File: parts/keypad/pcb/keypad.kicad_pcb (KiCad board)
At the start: 2 copper layers, 95 x 74.5 mm, 22 parts, among them J1 Conn_02x10_Top_Bottom, J2 1x10, J3 To SENSOR HUB, J4 To DISPLAY MODULE, SW1 SW_Push, SW10 SW_Push, SW2 SW_Push, SW3 SW_Push, SW4 SW_Push, SW5 SW_Push, SW6 SW_Push, SW7 SW_Push, SW8 SW_Push, SW9 SW_Push

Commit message: update connector to hub to match hub pinouts
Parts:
- removed J3: To SENSOR HUB, Connector_PinHeader_2.54mm:PinHeader_1x04_P2.54mm_Horizontal
- added TO_HUB1: Conn_01x05, Connector_PinHeader_2.54mm:PinHeader_1x05_P2.54mm_Horizontal, B.Cu at (56.8, 96.2)
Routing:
- net Net-(J2-SCL): track 107.3 -> 94.9 mm, vias 1 -> 0
- net /N$3: track 61.2 -> 52.3 mm, vias 1 -> 0
- net /GND: track 298.3 -> 290.0 mm, vias 0 -> 1
- net /N$2: track 81.3 -> 76.0 mm
- net Net-(J2-SDA): track 95.0 -> 91.8 mm
- net /N$5: track 93.9 -> 97.0 mm
- net Net-(J2-3V3): track 124.3 -> 121.5 mm
- net /N$10: track 18.8 -> 16.6 mm
- net /N$8: track 58.5 -> 56.4 mm
- net /N$9: track 24.1 -> 25.2 mm
- net /N$6: track 77.5 -> 76.7 mm
- net /N$1: track 99.0 -> 99.5 mm
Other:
- board text added: "(C) 2026 ARKADIA HOUSE Keypad Display rev 01.7"
- board text added: "3V3 nc GND SDA SCL"
- board text added: "To HUB"
- board text removed: "(C) 2026 ARKADIA HOUSE Keypad Display rev 01.6"
- board text removed: "SCL SDA 3V3 GND"

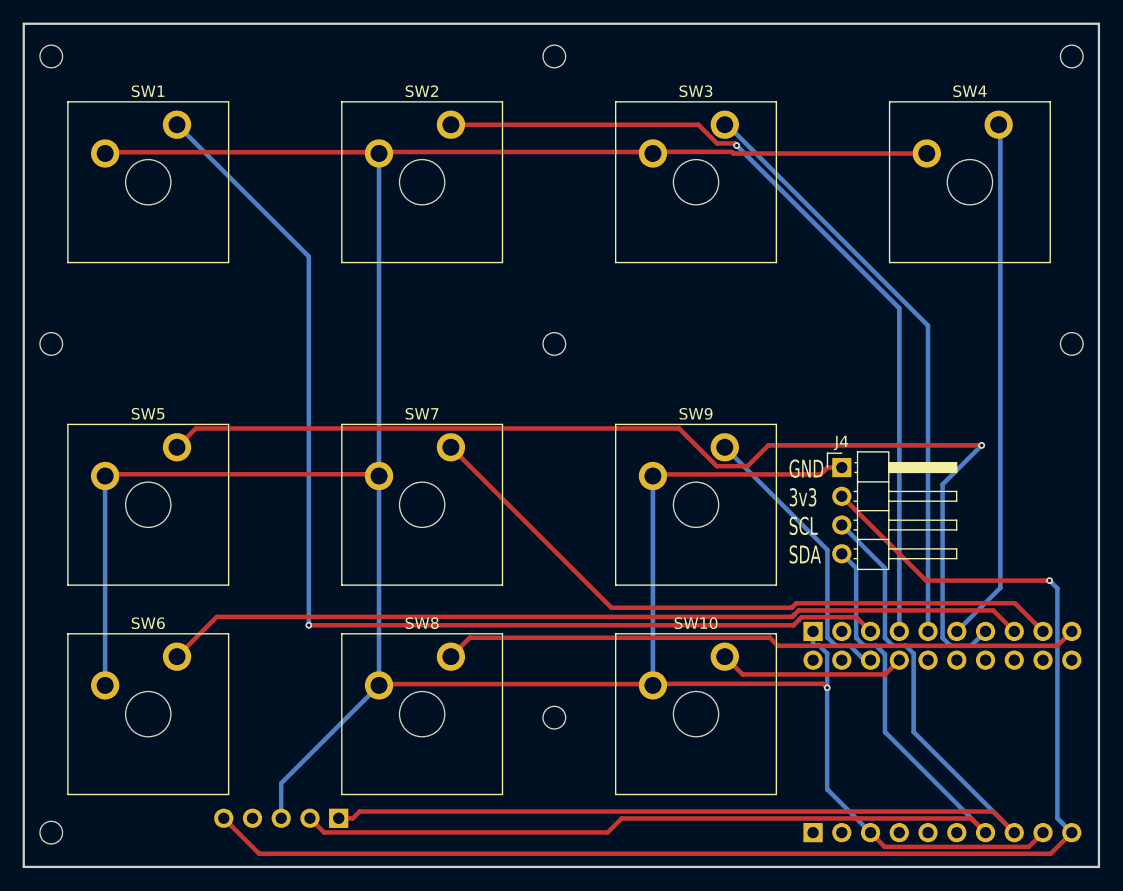
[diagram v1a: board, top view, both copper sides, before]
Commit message: cleaned up vias and tracks
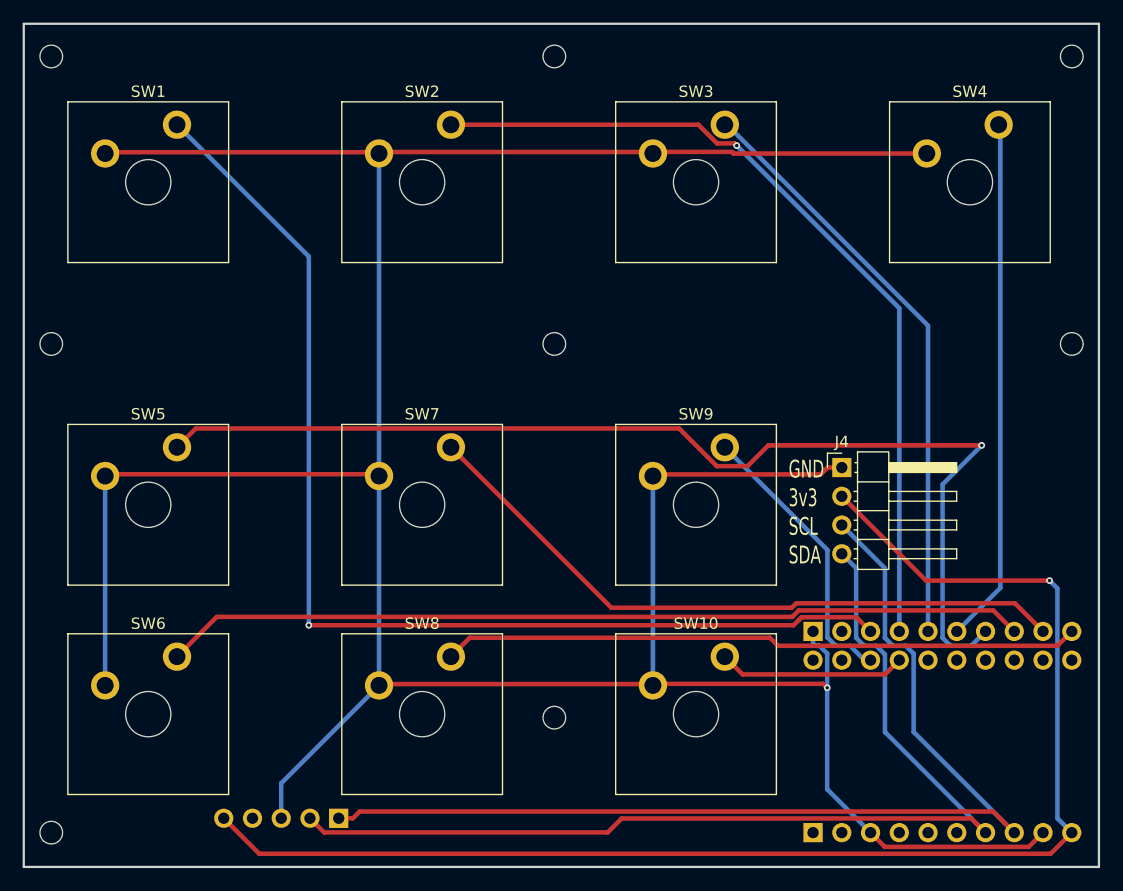
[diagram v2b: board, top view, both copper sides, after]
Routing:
- net /GND: track 290.0 -> 287.9 mm
- net /N$2: track 76.0 -> 74.9 mm
- net /N$9: track 25.2 -> 24.7 mm
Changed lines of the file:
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@@
 			(crossoutdnponfab yes)
 			(subtractmaskfromsilk no)
-			(outputformat 3)
+			(outputformat 1)
 			(mirror no)
-			(drillshape 2)
+			(drillshape 0)
 			(scaleselection 1)
 			(outputdirectory "../fab/")
@@
 	)
 	(segment
-		(start 84.7282 84.3218)
-		(end 84.59 84.46)
-		(width 0.4)
-		(layer "F.Cu")
-		(net "/GND")
-	)
-	(segment
 		(start 84.7282 37.3218)
 		(end 91.5627 37.3218)
@@
 	)
 	(segment
-		(start 60.5239 37.3261)
-		(end 60.39 37.46)
-		(width 0.4)
-		(layer "F.Cu")
-		(net "/GND")
-	)
-	(segment
 		(start 84.7363 65.8137)
 		(end 99.4266 65.8137)
@@
 	)
 	(segment
-		(start 84.59 65.96)
-		(end 84.7363 65.8137)
-		(width 0.4)
-		(layer "F.Cu")
-		(net "/GND")
-	)
-	(segment
 		(start 101.28 65.212)
 		(end 100.0283 65.212)
@@
 	)
 	(segment
-		(start 84.4783 84.3483)
-		(end 84.59 84.46)
-		(width 0.4)
-		(layer "F.Cu")
-		(net "/GND")
-	)
-	(segment
 		(start 84.4561 37.3261)
 		(end 60.5239 37.3261)
@@
 	)
 	(segment
-		(start 60.39 84.46)
-		(end 60.5017 84.3483)
-		(width 0.4)
-		(layer "F.Cu")
-		(net "/GND")
-	)
-	(segment
-		(start 84.59 37.46)
-		(end 84.4561 37.3261)
-		(width 0.4)
-		(layer "F.Cu")
-		(net "/GND")
-	)
-	(segment
 		(start 60.5017 84.3483)
 		(end 84.4783 84.3483)
@@
 	)
 	(segment
-		(start 108.7834 37.4666)
-		(end 108.79 37.46)
-		(width 0.4)
-		(layer "F.Cu")
-		(net "/GND")
-	)
-	(segment
 		(start 99.6392 84.3218)
 		(end 84.7282 84.3218)
@@
 	)
 	(segment
-		(start 36.19 65.96)
-		(end 36.3483 65.8017)
-		(width 0.4)
-		(layer "F.Cu")
-		(net "/GND")
-	)
-	(segment
 		(start 99.9917 84.6743)
 		(end 99.6392 84.3218)
@@
 	)
 	(segment
-		(start 60.2317 65.8017)
-		(end 60.39 65.96)
-		(width 0.4)
-		(layer "F.Cu")
-		(net "/GND")
-	)
-	(segment
 		(start 36.3483 65.8017)
 		(end 60.2317 65.8017)
@@
 	)
 	(segment
-		(start 60.2783 37.3483)
-		(end 60.39 37.46)
-		(width 0.4)
-		(layer "F.Cu")
-		(net "/GND")
-	)
-	(segment
 		(start 91.5627 37.3218)
 		(end 91.7075 37.4666)
@@
 		(net "/GND")
 	)
-	(segment
-		(start 36.19 37.46)
-		(end 36.3017 37.3483)
-		(width 0.4)
-		(layer "F.Cu")
-		(net "/GND")
-	)
-	(segment
-		(start 84.59 37.46)
-		(end 84.7282 37.3218)
-		(width 0.4)
-		(layer "F.Cu")
-		(net "/GND")
-	)
 	(via
 		(at 99.9917 84.6743)
@@
 	)
 	(segment
-		(start 91.8048 36.5717)
-		(end 91.998 36.7649)
-		(width 0.4)
-		(layer "F.Cu")
-		(net "/N$2")
-	)
-	(segment
 		(start 90.2559 36.5717)
 		(end 91.8048 36.5717)
@@
 	)
 	(segment
-		(start 91.8048 36.5717)
-		(end 91.998 36.7649)
-		(width 0.4)
-		(layer "F.Cu")
-		(net "/N$2")
-	)
-	(segment
 		(start 91.998 36.7649)
 		(end 91.8048 36.5717)
@@
 	)
 	(segment
-		(start 91.998 36.7649)
-		(end 91.8048 36.5717)
-		(width 0.4)
-		(layer "B.Cu")
-		(net "/N$2")
-	)
-	(segment
-		(start 91.8048 36.5717)
-		(end 91.998 36.7649)
-		(width 0.4)
-		(layer "B.Cu")
-		(net "/N$2")
-	)
-	(segment
 		(start 106.36 51.1269)
 		(end 106.36 79.69)
@@
 	)
 	(segment
-		(start 91.1454 34.92)
-		(end 90.94 34.92)
-		(width 0.4)
-		(layer "B.Cu")
-		(net "/N$3")
-	)
-	(segment
 		(start 108.9 79.69)
 		(end 108.9 52.6746)
@@
 	)
 	(segment
-		(start 115.2853 35.0653)
-		(end 115.14 34.92)
-		(width 0.4)
-		(layer "B.Cu")
-		(net "/N$4")
-	)
-	(segment
 		(start 115.2853 75.8447)
 		(end 115.2853 35.0653)
@@
 	)
 	(segment
-		(start 97.4745 77.8366)
-		(end 97.1219 78.1892)
-		(width 0.4)
-		(layer "F.Cu")
-		(net "/N$6")
-	)
-	(segment
 		(start 116.52 79.69)
 		(end 114.6666 77.8366)
@@
 	)
 	(segment
-		(start 97.1219 78.1892)
-		(end 96.9021 78.409)
-		(width 0.4)
-		(layer "F.Cu")
-		(net "/N$6")
-	)
-	(segment
 		(start 46.051 78.409)
 		(end 42.54 81.92)
@@
 	)
 	(segment
-		(start 97.1219 78.1892)
-		(end 96.9021 78.409)
+		(start 96.9021 78.409)
+		(end 97.4745 77.8366)
 		(width 0.4)
 		(layer "F.Cu")
@@
 	)
 	(segment
-		(start 96.8728 77.5875)
-		(end 96.8634 77.5969)
-		(width 0.4)
-		(layer "F.Cu")
-		(net "/N$7")
-	)
-	(segment
 		(start 119.06 79.69)
 		(end 116.5771 77.2071)
@@
 	)
 	(segment
-		(start 96.8728 77.5875)
-		(end 96.8634 77.5969)
+		(start 96.8634 77.5969)
+		(end 97.2532 77.2071)
 		(width 0.4)
 		(layer "F.Cu")
@@
 	)
 	(segment
-		(start 97.2532 77.2071)
-		(end 96.8728 77.5875)
-		(width 0.4)
-		(layer "F.Cu")
-		(net "/N$7")
-	)
-	(segment
 		(start 101.28 67.752)
 		(end 108.73 75.202)
@@
 	)
 	(segment
-		(start 103.2775 82.23)
-		(end 103.82 82.23)
-		(width 0.4)
-		(layer "B.Cu")
-		(net "/N$9")
-	)
-	(segment
